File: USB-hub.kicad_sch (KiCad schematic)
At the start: 11 parts, among them U302 CH334P, Y900 12Mhz

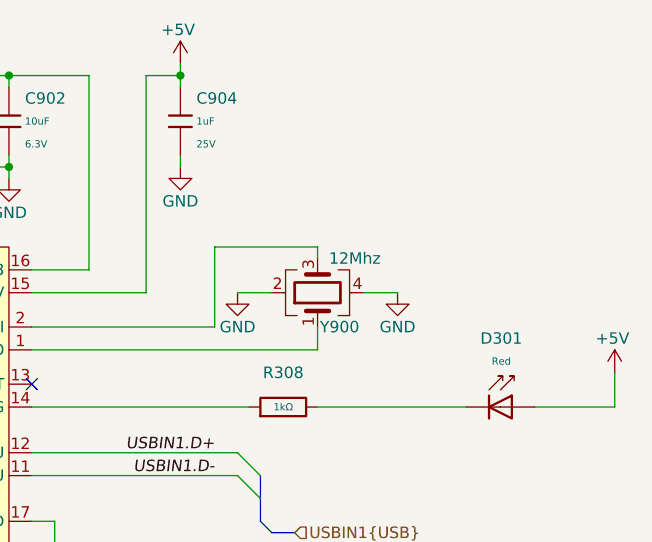
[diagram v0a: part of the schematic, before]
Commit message: Change MCU and update library
Changed MCU from H7 to H5 series due to programming issues with external
loader. Also updated JLCPCB components (not all tho there are still
arround 18 components to fix)
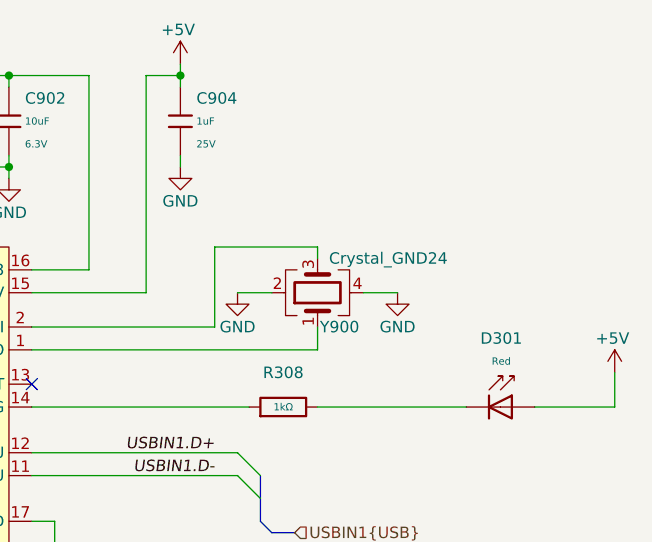
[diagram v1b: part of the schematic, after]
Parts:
- C900: Stock 3851753 -> 5436546
- C902: Price 0.007USD -> 0.008USD; Stock 7825129 -> 1226257
- C904: Stock 6814914 -> 6453835
- D301: Stock 2282993 -> 3289269
- R308: Stock 10672962 -> 7947916
- R900, R901, R902, R903: Stock 2497993 -> 2158519
- Y900: value 12Mhz -> Crystal_GND24
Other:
- title: ModuCard base module -> ModuCard BM STM32H562VGT6
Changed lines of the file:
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@@
 (kicad_sch
-	(version 20231120)
+	(version 20250114)
 	(generator "eeschema")
-	(generator_version "8.0")
+	(generator_version "9.0")
 	(paper "A4")
 	(title_block
-		(title "ModuCard base module")
-		(date "2025-02-25")
-		(rev "1.0.1")
+		(title "ModuCard BM STM32H562VGT6")
+		(date "2025-04-18")
+		(rev "1.0.0")
 		(company "KoNaR")
 		(comment 1 "Base project authors: Dominik Pluta, Artem Horiunov")
@@
 		(members "D+" "D-")
 	)
+	(text "USB HUB TO MCU AND STLINK"
+		(exclude_from_sim no)
+		(at 103.632 68.072 0)
+		(effects
+			(font
+				(size 1.27 1.27)
+			)
+		)
+	)
 	(junction
 		(at 162.56 48.26)
@@
 		)
 	)
-	(text "USB HUB TO MCU AND STLINK"
-		(exclude_from_sim no)
-		(at 103.632 68.072 0)
-		(effects
-			(font
-				(size 1.27 1.27)
-			)
-		)
-	)
 	(label "USBIN1.D-"
 		(at 166.37 92.71 180)
@@
 			)
 		)
-		(property "Stock" "2497993"
+		(property "Stock" "2158519"
 			(at 96.52 86.36 0)
 			(effects
@@
 		(on_board yes)
 		(dnp no)
-		(property "Reference" "#PWR0901"
+		(property "Reference" "#PWR901"
 			(at 186.69 78.74 0)
 			(effects
@@
 			)
 		)
-		(property "Description" ""
+		(property "Description" "Power symbol creates a global label with name \"GND\" , ground"
 			(at 186.69 72.39 0)
 			(effects
@@
 			(project "base-module"
 				(path "/090a8e41-87a8-4fb1-998b-60a2c0dc4cee/c4e62f69-aed8-45c4-bc74-414bd9b2dcad"
-					(reference "#PWR0901")
+					(reference "#PWR901")
 					(unit 1)
 				)
@@
 		(on_board yes)
 		(dnp no)
-		(property "Reference" "#PWR0905"
+		(property "Reference" "#PWR905"
 			(at 143.51 66.04 0)
 			(effects
@@
 			)
 		)
-		(property "Description" ""
+		(property "Description" "Power symbol creates a global label with name \"GND\" , ground"
 			(at 143.51 59.69 0)
 			(effects
@@
 			(project "base-module"
 				(path "/090a8e41-87a8-4fb1-998b-60a2c0dc4cee/c4e62f69-aed8-45c4-bc74-414bd9b2dcad"
-					(reference "#PWR0905")
+					(reference "#PWR905")
 					(unit 1)
 				)
@@
 			)
 		)
-		(property "Stock" "3851753"
+		(property "Stock" "5436546"
 			(at 133.35 53.34 0)
 			(effects
@@
 			)
 		)
-		(property "Stock" "6814914"
+		(property "Stock" "6453835"
 			(at 162.56 53.34 0)
 			(effects
@@
 			)
 		)
-		(property "Stock" "2497993"
+		(property "Stock" "2158519"
 			(at 96.52 95.25 0)
 			(effects
@@
 			)
 		)
-		(property "Stock" "2497993"
+		(property "Stock" "2158519"
 			(at 96.52 97.79 0)
 			(effects
@@
 			)
 		)
-		(property "Stock" "2497993"
+		(property "Stock" "2158519"
 			(at 96.52 88.9 0)
 			(effects
@@
 	)
 	(symbol
-		(lib_name "GND_1")
 		(lib_id "power:GND")
 		(at 148.59 101.6 0)
@@
 		(on_board yes)
 		(dnp no)
-		(property "Reference" "#PWR0329"
+		(property "Reference" "#PWR329"
 			(at 148.59 107.95 0)
 			(effects
@@
 			(project ""
 				(path "/090a8e41-87a8-4fb1-998b-60a2c0dc4cee/c4e62f69-aed8-45c4-bc74-414bd9b2dcad"
-					(reference "#PWR0329")
+					(reference "#PWR329")
 					(unit 1)
 				)
@@
 			)
 		)
-		(property "Stock" "2282993"
+		(property "Stock" "3289269"
 			(at 198.12 85.09 0)
 			(effects
@@
 			)
 		)
-		(property "Stock" "7825129"
+		(property "Stock" "1226257"
 			(at 143.51 53.34 0)
 			(effects
@@
 			)
 		)
-		(property "Price" "0.007USD"
+		(property "Price" "0.008USD"
 			(at 143.51 53.34 0)
 			(effects
@@
 		(on_board yes)
 		(dnp no)
-		(property "Reference" "#PWR0902"
+		(property "Reference" "#PWR902"
 			(at 162.56 50.8 0)
 			(effects
@@
 			(project "base-module"
 				(path "/090a8e41-87a8-4fb1-998b-60a2c0dc4cee/c4e62f69-aed8-45c4-bc74-414bd9b2dcad"
-					(reference "#PWR0902")
+					(reference "#PWR902")
 					(unit 1)
 				)
@@
 		(on_board yes)
 		(dnp no)
-		(property "Reference" "#PWR0904"
+		(property "Reference" "#PWR904"
 			(at 162.56 64.77 0)
 			(effects
@@
 			)
 		)
-		(property "Description" ""
+		(property "Description" "Power symbol creates a global label with name \"GND\" , ground"
 			(at 162.56 58.42 0)
 			(effects
@@
 			(project "base-module"
 				(path "/090a8e41-87a8-4fb1-998b-60a2c0dc4cee/c4e62f69-aed8-45c4-bc74-414bd9b2dcad"
-					(reference "#PWR0904")
+					(reference "#PWR904")
 					(unit 1)
 				)
@@
 		(on_board yes)
 		(dnp no)
-		(property "Reference" "#PWR0900"
+		(property "Reference" "#PWR900"
 			(at 168.91 78.74 0)
 			(effects
@@
 			)
 		)
-		(property "Description" ""
+		(property "Description" "Power symbol creates a global label with name \"GND\" , ground"
 			(at 168.91 72.39 0)
 			(effects
@@
 			(project "base-module"
 				(path "/090a8e41-87a8-4fb1-998b-60a2c0dc4cee/c4e62f69-aed8-45c4-bc74-414bd9b2dcad"
-					(reference "#PWR0900")
+					(reference "#PWR900")
 					(unit 1)
 				)
@@
 			)
 		)
-		(property "Stock" "10672962"
+		(property "Stock" "7947916"
 			(at 173.99 85.09 0)
 			(effects
@@
 			)
 		)
-		(property "Value" "12Mhz"
+		(property "Value" "Crystal_GND24"
 			(at 179.07 68.58 90)
 			(effects
@@
 			)
 		)
-		(property "Description" ""
+		(property "Description" "Four pin crystal, GND on pins 2 and 4"
 			(at 177.8 72.39 0)
 			(effects
@@
 		(on_board yes)
 		(dnp no)
-		(property "Reference" "#PWR0328"
+		(property "Reference" "#PWR328"
 			(at 210.82 85.09 0)
 			(effects
@@
 			(project "base-module"
 				(path "/090a8e41-87a8-4fb1-998b-60a2c0dc4cee/c4e62f69-aed8-45c4-bc74-414bd9b2dcad"
-					(reference "#PWR0328")
+					(reference "#PWR328")
 					(unit 1)
 				)

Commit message: [REV2] board finshed, schematics and leyout
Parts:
- added R416, R418: 22Ω, PCM_JLCPCB:R_0402, symbol PCM_JLCPCB-Resistors:0402,22Ω
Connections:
- net USB_GPS_.D-: now reaches U302.7 (DM2)
- net USB_GPS_.D-: now also R416.2
- net USB_GPS_.D+: now reaches U302.8 (DP2)
- net USB_GPS_.D+: now also R418.2
- new net USB_GPS.D+: R418.1
- new net USB_GPS.D-: R416.1
- no-connect marks 5 -> 3
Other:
- title: ModuCard BM STM32H562VGT6 -> ModuCard nav module
